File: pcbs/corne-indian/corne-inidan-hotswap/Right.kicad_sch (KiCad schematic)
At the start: 68 parts, among them U4 AP2127K-3.3, U5 RP2040, U6 W25Q32JVSS, Y2 12Mhz

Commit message: Mid of the renumbering & renaming
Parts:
- added rJ1: Conn_01x03_Pin, Connector_PinHeader_2.54mm:PinHeader_1x03_P2.54mm_Vertical, symbol Connector:Conn_01x03_Pin
- added rJ2: Conn_01x04_Pin, Connector_PinHeader_2.54mm:PinHeader_1x04_P2.54mm_Vertical, symbol Connector:Conn_01x04_Pin
- added rR7: 10K, Resistor_SMD:R_0603_1608Metric, symbol Device:R
- renumbered C12 to rC1, C21 to rC10, C22 to rC11, C13 to rC2, C14 to rC3, C15 to rC4, C16 to rC5, C17 to rC6, C18 to rC7, C19 to rC8, C20 to rC9, D2 to rD1, MCU2 to rMCU1, R7 to rR1, R8 to rR2, R9 to rR3, R10 to rR4, R11 to rR5, R12 to rR6, TP4 to rTP1, U4 to rU1, U5 to rU2, U6 to rU3, Y2 to rY1
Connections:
- net GPIO_00 is gone; now on net KEY_4: rU2.2 (GPIO0)
- net GPIO_01 is gone; now on net KEY_6: rU2.3 (GPIO1)
- net GPIO_02 is gone; now on net KEY_3: rU2.4 (GPIO2)
- net GPIO_03 is gone; now on net KEY_7: rU2.5 (GPIO3)
- net GPIO_09 is gone; now on net KEY_2: rU2.12 (GPIO9)
- net GPIO_11 is gone; now on net KEY_1: rU2.14 (GPIO11)
- net GPIO_14 is gone; now on net KEY_9: rU2.17 (GPIO14)
- net GPIO_15 is gone; now on net KEY_8: rU2.18 (GPIO15)
- net GPIO_16 is gone; now on net KEY_16: rU2.27 (GPIO16)
- net GPIO_17 is gone; now on net KEY_21: rU2.28 (GPIO17)
- net GPIO_18 is gone; now on net KEY_17: rU2.29 (GPIO18)
- net GPIO_19 is gone; now on net KEY_20: rU2.30 (GPIO19)
- net GPIO_20 is gone; now on net KEY_18: rU2.31 (GPIO20)
- net GPIO_22 is gone; now on net KEY_19: rU2.34 (GPIO22)
- net GPIO_23 is gone; now on net KEY_13: rU2.35 (GPIO23)
- net GPIO_24 is gone; now on net KEY_14: rU2.36 (GPIO24)
- net GPIO_25 is gone; now on net KEY_15: rU2.37 (GPIO25)
- net GPIO_26 is gone; now on net KEY_12: rU2.38 (GPIO26_ADC0)
- net GPIO_27 is gone; now on net KEY_11: rU2.39 (GPIO27_ADC1)
- net GPIO_28 is gone; now on net KEY_10: rU2.40 (GPIO28_ADC2)
- net GPIO_29 is gone; now on net KEY_5: rU2.41 (GPIO29_ADC3)
- net D+: now also rR3.2; no longer TP6.1, rR4.2
- net D-: now also rR4.2; no longer TP5.1, rR3.2
- net GND: now also rR7.2
- net U_+: now also TP6.1; no longer rR4.1
- net U_-: now also TP5.1; no longer rR3.1
- net GPIO_04: no longer names the net of rU2.6 (GPIO4)
- net GPIO_05: no longer names the net of rU2.7 (GPIO5)
- net GPIO_06: no longer names the net of rU2.8 (GPIO6)
- net GPIO_07: no longer names the net of rU2.9 (GPIO7)
- net GPIO_08: no longer names the net of rU2.11 (GPIO8)
- net GPIO_10: no longer names the net of rU2.13 (GPIO10)
- net GPIO_12: no longer names the net of rU2.15 (GPIO12)
- net GPIO_13: no longer names the net of rU2.16 (GPIO13)
- net GPIO_21: no longer names the net of rU2.32 (GPIO21)
- net GPIO_21: now also rR7.1
- new net U+: rR3.1
- new net U-: rR4.1
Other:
- note added: "Flash Memory"
- note added: "MCU RP2040"
- note added: "SPLIT_HAND_PIN"
- moved on the sheet: TP5, TP6, rC1, rC10, rC11, rC2, rC3, rC4, rC5, rC6, rC7, rC8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

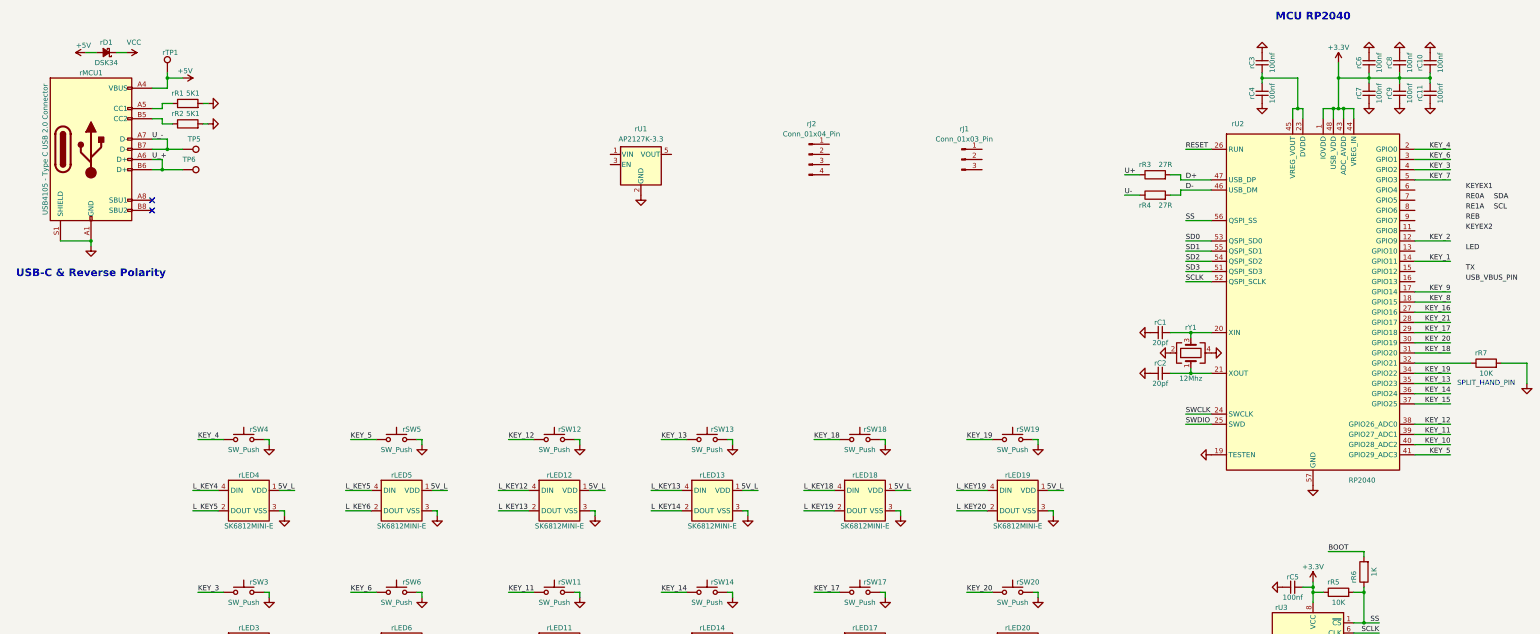
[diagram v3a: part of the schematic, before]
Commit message: Mid of the Placement still Rotary encoder is not done
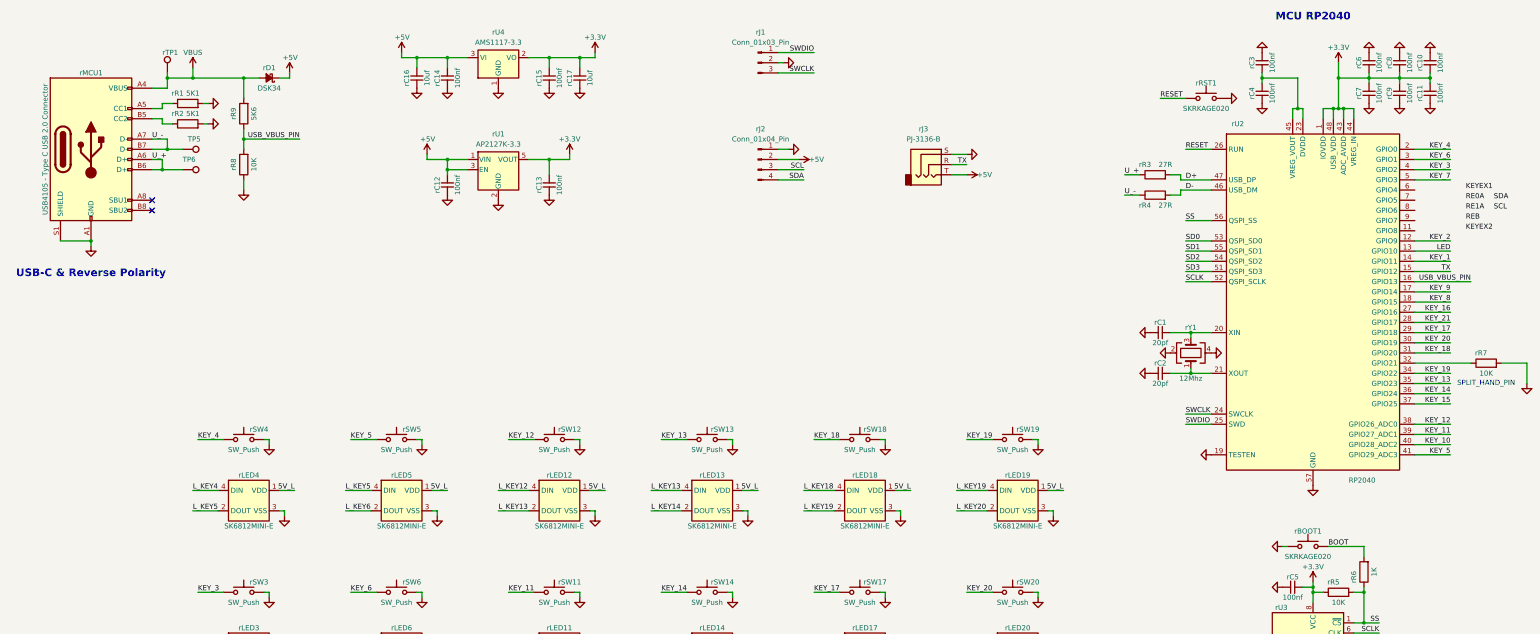
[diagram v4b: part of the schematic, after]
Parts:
- added rBOOT1, rRST1: SKRKAGE020, Button:SW_Push_SPST_NO_Alps_SKRK, symbol Switch:SW_Push
- added rC12, rC13, rC14, rC15: 100nf, Capacitor_SMD:C_0603_1608Metric, symbol Device:C_Small
- added rC16, rC17: 10uf, Capacitor_SMD:C_0603_1608Metric, symbol Device:C_Small
- added rJ3: PJ-3136-B, Conn_Audio:PJ-3136-B, symbol Connector_Audio:AudioJack3
- added rR8: 10K, Resistor_SMD:R_0603_1608Metric, symbol Device:R
- added rR9: 5K6, Resistor_SMD:R_0603_1608Metric, symbol Device:R
- added rU4: AMS1117-3.3, Package_TO_SOT_SMD:SOT-223-3_TabPin2, symbol Regulator_Linear:AMS1117-3.3
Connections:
- net U+ is gone; now on net U_+: rR3.1
- net U- is gone; now on net U_-: rR4.1
- net VCC is gone; now on net +5V: rD1.1 (K)
- net +3.3V: now also rU1.5 (VOUT), rC13.2, rC15.2, rC17.2, rU4.2 (VO)
- net +5V: now also rJ2.2 (Pin_2), rU1.1 (VIN), rU1.3 (EN), rC12.2, rC14.2, rC16.2, rJ3.T, rU4.3 (VI); no longer rD1.2 (A), rMCU1.A4 (VBUS), rMCU1.A9 (VBUS), rMCU1.B4 (VBUS), rMCU1.B9 (VBUS), rTP1.1
- net BOOT: now also rBOOT1.1
- net GND: now also rJ1.2 (Pin_2), rJ2.1 (Pin_1), rBOOT1.2, rC12.1, rC13.1, rC14.1, rC15.1, rC16.1, rC17.1, rJ3.S, rR8.1, rRST1.2, rU4.1 (GND)
- net LED: now also rU2.13 (GPIO10)
- net RESET: now also rRST1.1
- net SCL: now also rJ2.3 (Pin_3)
- net SDA: now also rJ2.4 (Pin_4)
- net SWCLK: now also rJ1.3 (Pin_3)
- net SWDIO: now also rJ1.1 (Pin_1)
- net TX: now also rU2.15 (GPIO12), rJ3.R
- net USB_VBUS_PIN: now also rU2.16 (GPIO13), rR8.2, rR9.1
- new net VBUS: rD1.2 (A), rMCU1.A4 (VBUS), rMCU1.A9 (VBUS), rMCU1.B4 (VBUS), rMCU1.B9 (VBUS), rR9.2, rTP1.1

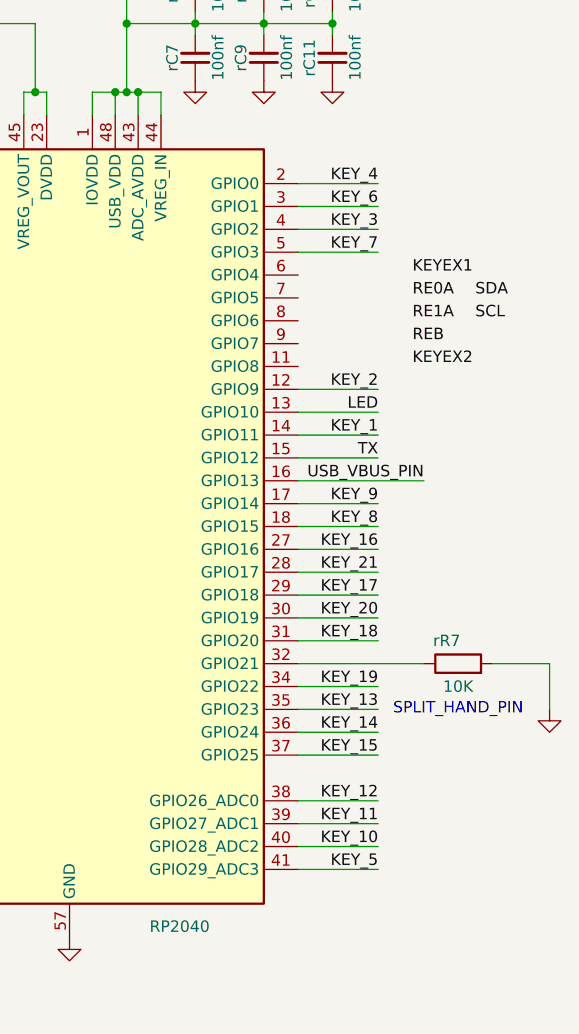
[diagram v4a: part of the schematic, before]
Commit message: Mid of the Component placement still the Rotarty nob is not done
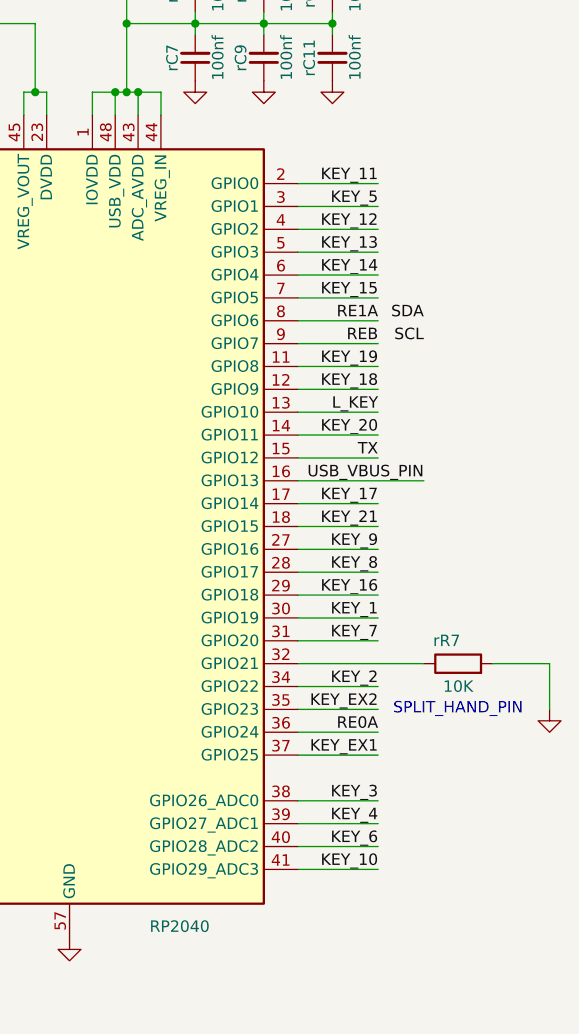
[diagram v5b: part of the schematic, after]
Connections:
- net LED is gone; now on net L_KEY: rU2.13 (GPIO10)
- net KEY_1: now also rU2.30 (GPIO19); no longer rU2.14 (GPIO11)
- net KEY_10: now also rU2.41 (GPIO29_ADC3); no longer rU2.40 (GPIO28_ADC2)
- net KEY_11: now also rU2.2 (GPIO0); no longer rU2.39 (GPIO27_ADC1)
- net KEY_12: now also rU2.4 (GPIO2); no longer rU2.38 (GPIO26_ADC0)
- net KEY_13: now also rU2.5 (GPIO3); no longer rU2.35 (GPIO23)
- net KEY_14: now also rU2.6 (GPIO4); no longer rU2.36 (GPIO24)
- net KEY_15: now also rU2.7 (GPIO5); no longer rU2.37 (GPIO25)
- net KEY_16: now also rU2.29 (GPIO18); no longer rU2.27 (GPIO16)
- net KEY_17: now also rU2.17 (GPIO14); no longer rU2.29 (GPIO18)
- net KEY_18: now also rU2.12 (GPIO9); no longer rU2.31 (GPIO20)
- net KEY_19: now also rU2.11 (GPIO8); no longer rU2.34 (GPIO22)
- net KEY_2: now also rU2.34 (GPIO22); no longer rU2.12 (GPIO9)
- net KEY_20: now also rU2.14 (GPIO11); no longer rU2.30 (GPIO19)
- net KEY_21: now also rU2.18 (GPIO15); no longer rU2.28 (GPIO17)
- net KEY_3: now also rU2.38 (GPIO26_ADC0); no longer rU2.4 (GPIO2)
- net KEY_4: now also rU2.39 (GPIO27_ADC1); no longer rU2.2 (GPIO0)
- net KEY_5: now also rU2.3 (GPIO1); no longer rU2.41 (GPIO29_ADC3)
- net KEY_6: now also rU2.40 (GPIO28_ADC2); no longer rU2.3 (GPIO1)
- net KEY_7: now also rU2.31 (GPIO20); no longer rU2.5 (GPIO3)
- net KEY_8: now also rU2.28 (GPIO17); no longer rU2.18 (GPIO15)
- net KEY_9: now also rU2.27 (GPIO16); no longer rU2.17 (GPIO14)
- net RE0A: now also rU2.36 (GPIO24)
- net RE1A: now also rU2.8 (GPIO6)
- net REB: now also rU2.9 (GPIO7)
- new net KEY_EX1: rU2.37 (GPIO25)
- new net KEY_EX2: rU2.35 (GPIO23)
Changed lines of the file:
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@@
 	(wire
 		(pts
+			(xy 368.3 64.77) (xy 377.19 64.77)
+		)
+		(stroke
+			(width 0)
+			(type default)
+		)
+	)
+	(wire
+		(pts
 			(xy 119.38 31.75) (xy 119.38 34.29)
 		)
@@
 	(wire
 		(pts
+			(xy 368.3 69.85) (xy 377.19 69.85)
+		)
+		(stroke
+			(width 0)
+			(type default)
+		)
+	)
+	(wire
+		(pts
 			(xy 364.49 36.83) (xy 372.11 36.83)
 		)
@@
 	(wire
 		(pts
+			(xy 368.3 67.31) (xy 377.19 67.31)
+		)
+		(stroke
+			(width 0)
+			(type default)
+		)
+	)
+	(wire
+		(pts
 			(xy 46.99 254) (xy 50.8 254)
 		)
@@
 	(wire
 		(pts
+			(xy 368.3 72.39) (xy 377.19 72.39)
+		)
+		(stroke
+			(width 0)
+			(type default)
+		)
+	)
+	(wire
+		(pts
 			(xy 356.87 36.83) (xy 356.87 38.1)
 		)
@@
 	(wire
 		(pts
+			(xy 368.3 74.93) (xy 377.19 74.93)
+		)
+		(stroke
+			(width 0)
+			(type default)
+		)
+	)
+	(wire
+		(pts
 			(xy 209.55 62.23) (xy 215.9 62.23)
 		)
@@
 		)
 	)
-	(label "KEY_9"
+	(label "KEY_17"
 		(at 377.19 90.17 180)
 		(effects
@@
 		)
 	)
-	(label "KEY_5"
+	(label "KEY_10"
 		(at 377.19 130.81 180)
 		(effects
@@
 		)
 	)
-	(label "KEYEX1"
-		(at 381 64.77 0)
+	(label "KEY_14"
+		(at 377.19 64.77 180)
 		(effects
 			(font
 				(size 1.27 1.27)
 			)
-			(justify left bottom)
+			(justify right bottom)
 		)
 	)
@@
 		)
 	)
-	(label "KEY_13"
+	(label "KEY_EX2"
 		(at 377.19 113.03 180)
 		(effects
@@
 		)
 	)
-	(label "KEY_12"
+	(label "KEY_3"
 		(at 377.19 123.19 180)
 		(effects
@@
 		)
 	)
-	(label "RE0A"
-		(at 381 67.31 0)
+	(label "KEY_15"
+		(at 377.19 67.31 180)
 		(effects
 			(font
 				(size 1.27 1.27)
 			)
-			(justify left bottom)
+			(justify right bottom)
 		)
 	)
-	(label "KEY_4"
+	(label "KEY_11"
 		(at 377.19 54.61 180)
 		(effects
@@
 		)
 	)
-	(label "KEY_14"
+	(label "RE0A"
 		(at 377.19 115.57 180)
 		(effects
@@
 		)
 	)
-	(label "KEY_16"
+	(label "KEY_9"
 		(at 377.19 95.25 180)
 		(effects
@@
 		)
 	)
-	(label "KEY_15"
+	(label "KEY_EX1"
 		(at 377.19 118.11 180)
 		(effects
@@
 		)
 	)
-	(label "KEY_2"
+	(label "KEY_18"
 		(at 377.19 77.47 180)
 		(effects
@@
 		)
 	)
-	(label "KEY_8"
+	(label "KEY_21"
 		(at 377.19 92.71 180)
 		(effects
@@
 		)
 	)
-	(label "KEY_11"
+	(label "KEY_4"
 		(at 377.19 125.73 180)
 		(effects
@@
 	)
 	(label "SCL"
-		(at 387.985 69.85 0)
+		(at 382.27 72.39 180)
 		(effects
 			(font
 				(size 1.27 1.27)
 			)
-			(justify left bottom)
+			(justify right bottom)
 		)
 	)
@@
 		)
 	)
-	(label "KEYEX2"
-		(at 381 74.93 0)
+	(label "KEY_19"
+		(at 377.19 74.93 180)
 		(effects
 			(font
 				(size 1.27 1.27)
 			)
-			(justify left bottom)
+			(justify right bottom)
 		)
 	)
@@
 		)
 	)
-	(label "KEY_10"
+	(label "KEY_6"
 		(at 377.19 128.27 180)
 		(effects
@@
 		)
 	)
-	(label "KEY_3"
+	(label "KEY_12"
 		(at 377.19 59.69 180)
 		(effects
@@
 		)
 	)
-	(label "KEY_18"
+	(label "KEY_7"
 		(at 377.19 105.41 180)
 		(effects
@@
 	)
 	(label "REB"
-		(at 381 72.39 0)
+		(at 377.19 72.39 180)
 		(effects
 			(font
 				(size 1.27 1.27)
 			)
-			(justify left bottom)
+			(justify right bottom)
 		)
 	)
-	(label "KEY_6"
+	(label "KEY_5"
 		(at 377.19 57.15 180)
 		(effects
@@
 		)
 	)
-	(label "KEY_20"
+	(label "KEY_1"
 		(at 377.19 102.87 180)
 		(effects
@@
 		)
 	)
-	(label "KEY_7"
+	(label "KEY_13"
 		(at 377.19 62.23 180)
 		(effects
@@
 	)
 	(label "SDA"
-		(at 387.985 67.31 0)
+		(at 382.27 69.85 180)
 		(effects
 			(font
 				(size 1.27 1.27)
 			)
-			(justify left bottom)
+			(justify right bottom)
 		)
 	)
@@
 		)
 	)
-	(label "KEY_1"
+	(label "KEY_20"
 		(at 377.19 82.55 180)
 		(effects
@@
 		)
 	)
-	(label "KEY_17"
+	(label "KEY_16"
 		(at 377.19 100.33 180)
 		(effects
@@
 		)
 	)
-	(label "LED"
+	(label "L_KEY"
 		(at 377.19 80.01 180)
 		(effects
@@
 		)
 	)
-	(label "KEY_19"
+	(label "KEY_2"
 		(at 377.19 110.49 180)
 		(effects
@@
 		)
 	)
-	(label "KEY_21"
+	(label "KEY_8"
 		(at 377.19 97.79 180)
 		(effects
@@
 	)
 	(label "RE1A"
-		(at 381 69.85 0)
+		(at 377.19 69.85 180)
 		(effects
 			(font
 				(size 1.27 1.27)
 			)
-			(justify left bottom)
+			(justify right bottom)
 		)
 	)

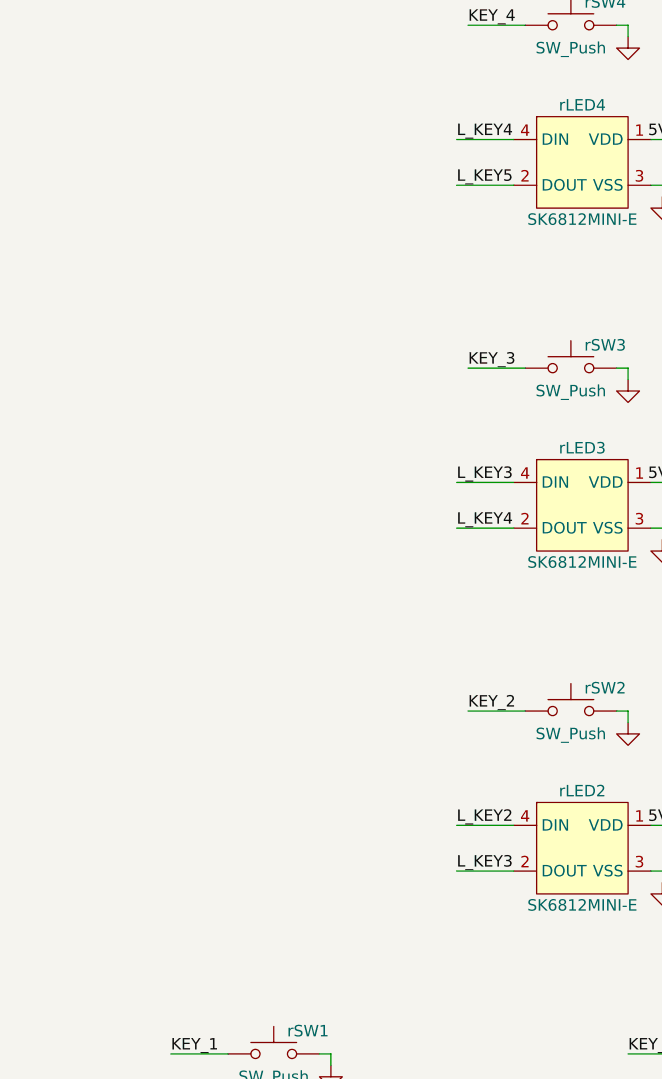
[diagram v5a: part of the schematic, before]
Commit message: Rotart encode also added in PCB layout
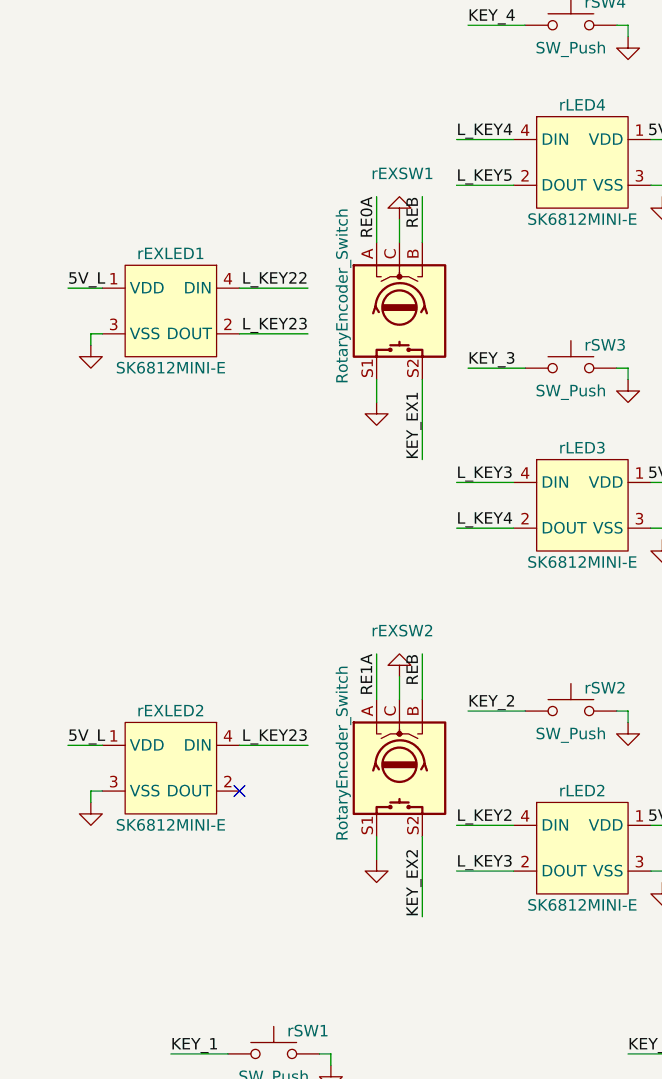
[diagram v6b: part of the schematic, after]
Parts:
- added rEXLED1, rEXLED2: SK6812MINI-E, User_Button_Switch_Keyboard:YS-SK6812MINI-E, symbol LED_RGB:LED_SK6812MINI-E
- added rEXSW1, rEXSW2: RotaryEncoder_Switch, User_Button_Switch_Keyboard:keyswitch_cherrymx_hotswap_1u_rotary_encoder_ec12, symbol Device:RotaryEncoder_Switch
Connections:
- net 5V_L: now also rEXLED1.1 (VDD), rEXLED2.1 (VDD)
- net GND: now also rEXLED1.3 (VSS), rEXLED2.3 (VSS), rEXSW1.C, rEXSW1.S1, rEXSW2.C, rEXSW2.S1
- net KEY_EX1: now also rEXSW1.S2
- net KEY_EX2: now also rEXSW2.S2
- net L_KEY22: now also rEXLED1.4 (DIN)
- net RE0A: now also rEXSW1.A
- net RE1A: now also rEXSW2.A
- net REB: now also rEXSW1.B, rEXSW2.B
- new net L_KEY23: rEXLED1.2 (DOUT), rEXLED2.4 (DIN)
- no-connect marks 2 -> 3

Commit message: Mid of the Layout
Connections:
- net SCL is gone; now on net REB: rJ2.3 (Pin_3)
- net SDA is gone; now on net RE1A: rJ2.4 (Pin_4)
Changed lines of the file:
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@@
 	(wire
 		(pts
-			(xy 368.3 69.85) (xy 377.19 69.85)
+			(xy 368.3 69.85) (xy 382.27 69.85)
 		)
 		(stroke
@@
 	(wire
 		(pts
-			(xy 368.3 72.39) (xy 377.19 72.39)
-		)
-		(stroke
+			(xy 368.3 72.39) (xy 382.27 72.39)
+		)
+		(stroke
